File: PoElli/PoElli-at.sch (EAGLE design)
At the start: 119 parts, among them J1 DF12-60DP, Q1 FDV301N, Q2 SI1307DL, T1 POE-ISOLATION, U1 FST3257, U3 NCP1117, X1 RJ45MOLEX, Y1 25MHz

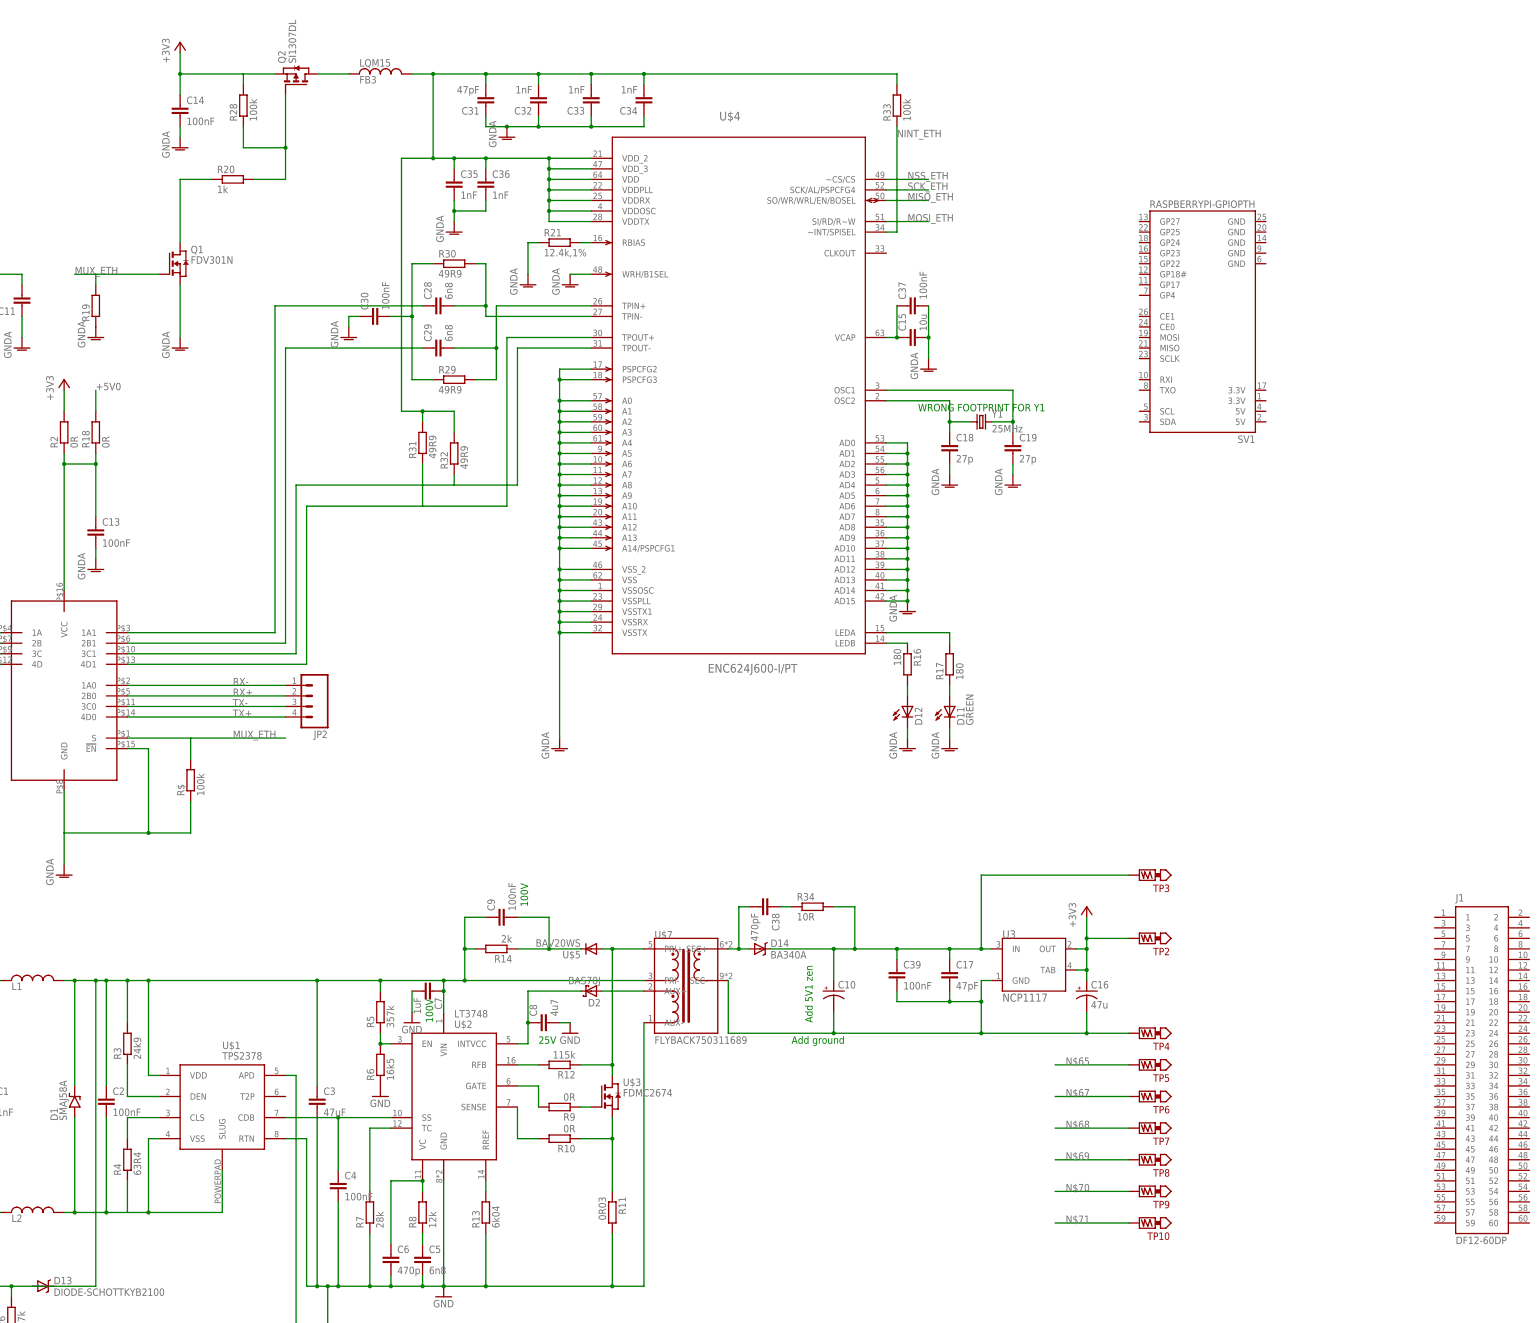
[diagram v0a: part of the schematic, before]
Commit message: Update and add wiring for ELL-i and RasPi connectors
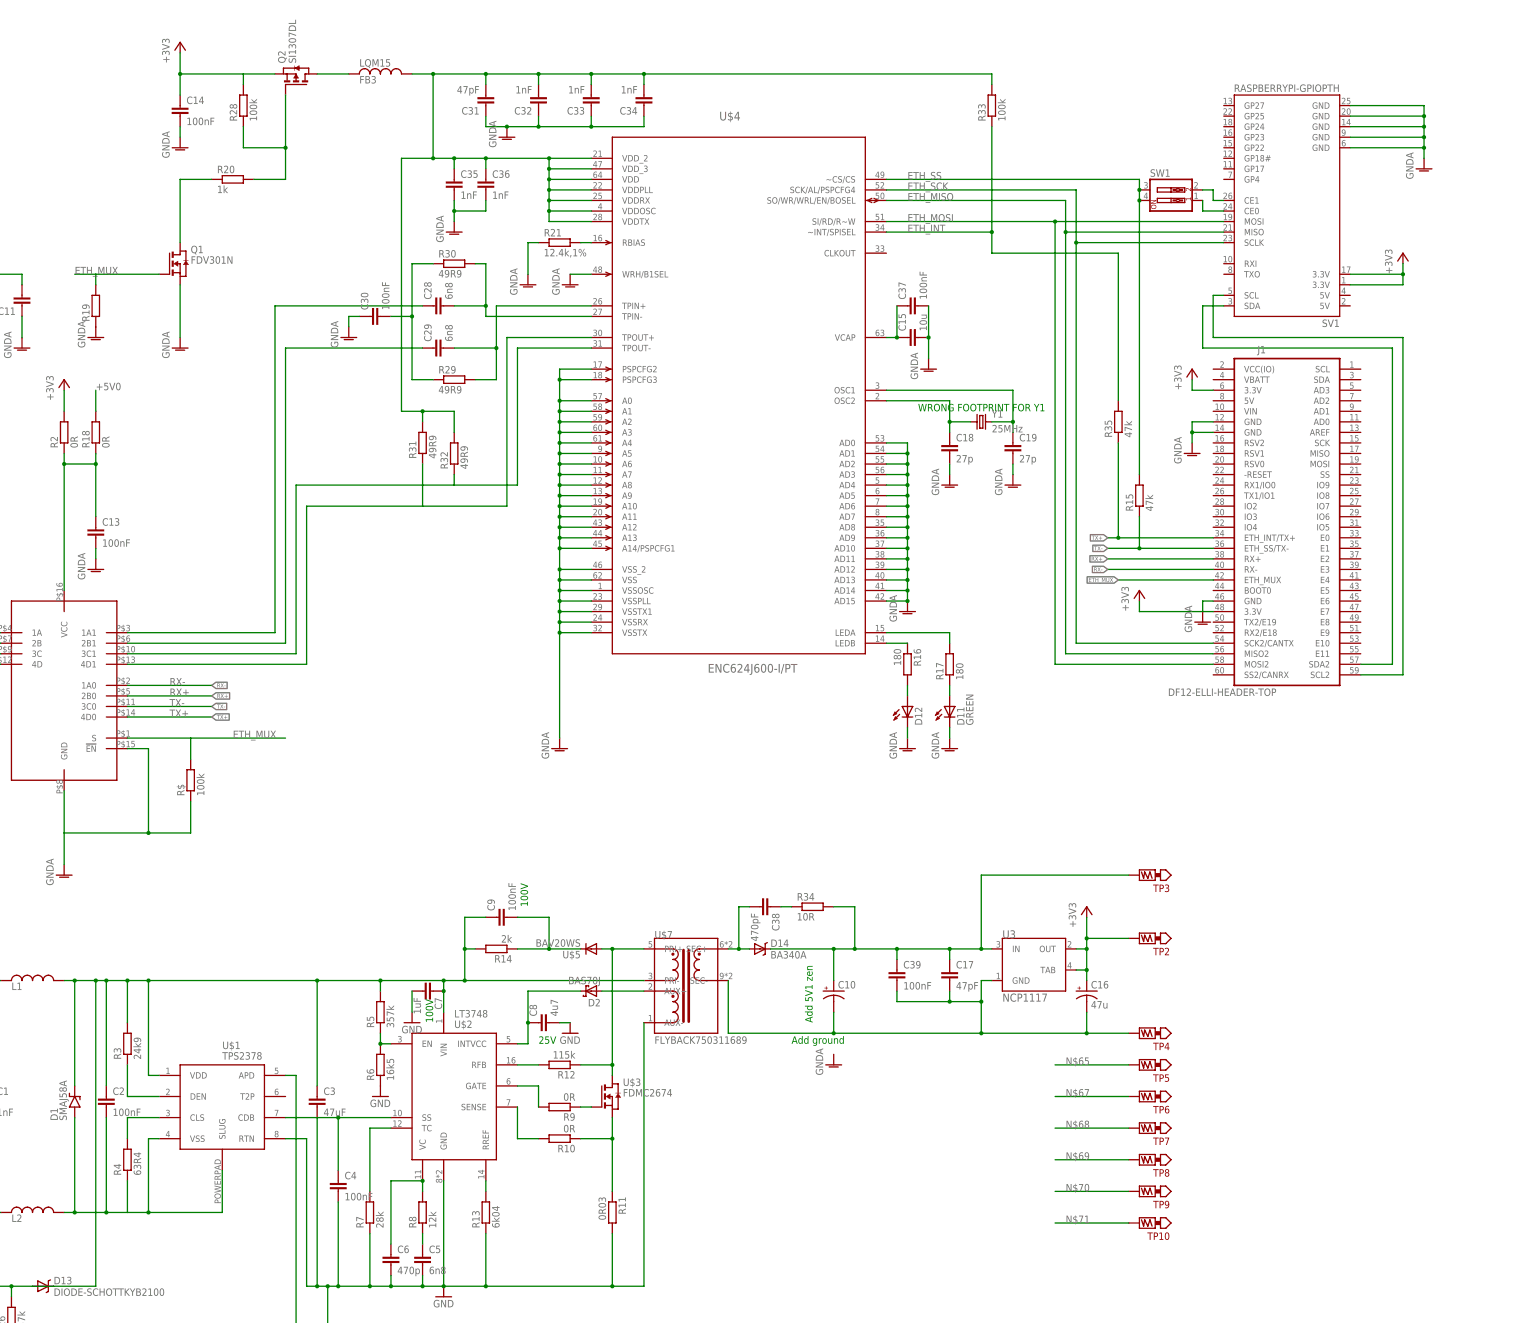
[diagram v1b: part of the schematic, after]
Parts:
- removed JP2: (no value), SparkFun-Connectors:M04LOCK
- added R15, R35: 47k, ELL-i-Passives:R0805
- added SW1: (no value), SparkFun-Electromechanical:SW_DIP-2-SMT-HALFSIZE
- J1: value DF12-60DP -> DF12-ELLI-HEADER-TOP; device ELL-i-Connectors:DF12-60DP -> ELL-i-Connectors:DF12-ELLI-HEADER-TOP
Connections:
- removed net MISO_ETH: U$4.SO/WR/WRL/EN/BOSEL
- removed net MOSI_ETH: U$4.SI/RD/R~W
- removed net MUX_ETH: Q1.G, R$.2, R19.2, U1.S
- removed net NINT_ETH: R33.1, U$4.~INT/SPISEL
- removed net NSS_ETH: U$4.~CS/CS
- removed net SCK_ETH: U$4.SCK/AL/PSPCFG4
- new net ETH_INT: R33.1, R35.2, U$4.~INT/SPISEL
- new net ETH_MISO: J1.MISO2, SV1.MISO, U$4.SO/WR/WRL/EN/BOSEL
- new net ETH_MOSI: J1.MOSI2, SV1.MOSI, U$4.SI/RD/R~W
- new net ETH_MUX: J1.ETH_MUX, Q1.G, R$.2, R19.2, U1.S
- new net ETH_SCK: J1.SCK2/CANTX, SV1.SCLK, U$4.SCK/AL/PSPCFG4
- new net ETH_SS: R15.2, SW1.3, SW1.4, U$4.~CS/CS
- new net N$72: J1.SDA2, SV1.SDA
- new net N$73: J1.SCL2, SV1.SCL
- new net N$74: SV1.CE1, SW1.2
- new net N$75: SV1.CE0, SW1.1
- net +3V3: now also J1.3.3V@48, J1.3.3V@6, SV1.3.3V@1, SV1.3.3V@17
- net GNDA: now also J1.GND@12, J1.GND@14, J1.GND@46, SV1.GND@14, SV1.GND@20, SV1.GND@25, SV1.GND@6, SV1.GND@9
- net RX+: now also J1.RX+; no longer JP2.2
- net RX-: now also J1.RX-; no longer JP2.1
- net TX+: now also J1.ETH_INT/TX+, R35.1; no longer JP2.4
- net TX-: now also J1.ETH_SS/TX-, R15.1; no longer JP2.3
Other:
- moved on the sheet: R33, SV1

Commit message: Cleanup PoElli-at aka Piwelli
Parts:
- D13: value DIODE-SCHOTTKYB2100 -> B2100
- T1: value POE-ISOLATION -> POE-ISOLATION-230NL; device ELL-i-Transformers:POE-ISOLATION -> ELL-i-Transformers:POE-ISOLATION-230NL
- X1: value RJ45MOLEX -> POE-TP-RJ45-MOLEX; device ELL-i-Connectors:RJ45MOLEX -> ELL-i-Connectors:POE-TP-RJ45-MOLEX
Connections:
- new net N$76: C26.1, D13.A, FB1.2, R26.2
- net N$1: now also T1.TX-, X1.TX-@2; no longer T1.TX1-, X1.2
- net N$16: no longer C26.1, D13.A, FB1.2, R26.2
- net N$2: now also T1.TX+, X1.TX+@1; no longer T1.TX1+, X1.1
- net N$3: now also T1.RX+, X1.RX+@3; no longer T1.RX1+, X1.3
- net N$4: now also X1.RX-@6; no longer X1.6
- net N$5: now also X1.POE-@7, X1.POE-@8; no longer X1.7, X1.8
- net N$7: now also X1.POE+@4, X1.POE+@5; no longer X1.4, X1.5
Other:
- moved on the sheet: C1, C10, C11, C12, C13, C14, C16, C17, C2, C20, C21, C22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

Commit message: Small fixes to PoElli
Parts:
- T1: value POE-ISOLATION-230NL -> Coilcraft 230NL
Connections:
- net +3V3: no longer SV1.3.3V@1, SV1.3.3V@17
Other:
- note added: "How about VCC(IO)? Set by MCU?"
- note added: "RasPi 3.3V must float"
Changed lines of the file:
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@@
 <part name="U$1" library="ELL-i-PowerIC" deviceset="TPS2378" device=""/>
 <part name="X1" library="ELL-i-Connectors" deviceset="POE-TP" device="-RJ45-MOLEX"/>
-<part name="T1" library="ELL-i-Transformers" deviceset="POE-ISOLATION" device="-230NL"/>
+<part name="T1" library="ELL-i-Transformers" deviceset="POE-ISOLATION" device="-230NL" value="Coilcraft 230NL"/>
 <part name="SV1" library="SparkFun-Boards" deviceset="RASPBERRYPI-GPIO" device="PTH"/>
 <part name="C1" library="ELL-i-Passives" deviceset="C" device="0805" value="1nF"/>
@@
 <part name="GND26" library="supply1" deviceset="GNDA" device=""/>
 <part name="GND27" library="supply1" deviceset="GNDA" device=""/>
-<part name="+3V5" library="supply1" deviceset="+3V3" device=""/>
 <part name="+3V6" library="supply1" deviceset="+3V3" device=""/>
 <part name="+3V7" library="supply1" deviceset="+3V3" device=""/>
@@
 <text x="322.58" y="73.66" size="1.778" layer="91">Add ground</text>
 <text x="327.66" y="78.74" size="1.778" layer="91" rot="R90">Add 5V1 zen</text>
+<text x="347.98" y="261.62" size="1.778" layer="97" align="center">RasPi 3.3V
+must float </text>
+<text x="294.64" y="243.84" size="1.778" layer="97" align="center">How about
+VCC(IO)?
+Set by MCU?</text>
 </plain>
 <instances>
@@
 <instance part="GND26" gate="1" x="302.26" y="177.8"/>
 <instance part="GND27" gate="1" x="299.72" y="218.44"/>
-<instance part="+3V5" gate="G$1" x="350.52" y="266.7"/>
 <instance part="+3V6" gate="G$1" x="299.72" y="238.76"/>
 <instance part="+3V7" gate="G$1" x="287.02" y="185.42"/>
@@
 </segment>
 <segment>
-<pinref part="SV1" gate="JP1" pin="3.3V@17"/>
-<wire x1="337.82" y1="261.62" x2="350.52" y2="261.62" width="0.1524" layer="91"/>
-<pinref part="+3V5" gate="G$1" pin="+3V3"/>
-<wire x1="350.52" y1="261.62" x2="350.52" y2="264.16" width="0.1524" layer="91"/>
-<pinref part="SV1" gate="JP1" pin="3.3V@1"/>
-<wire x1="337.82" y1="259.08" x2="350.52" y2="259.08" width="0.1524" layer="91"/>
-<wire x1="350.52" y1="259.08" x2="350.52" y2="261.62" width="0.1524" layer="91"/>
-<junction x="350.52" y="261.62"/>
-</segment>
-<segment>
 <pinref part="J1" gate="E" pin="3.3V@6"/>
 <wire x1="304.8" y1="233.68" x2="299.72" y2="233.68" width="0.1524" layer="91"/>
@@
 </schematic>
 </drawing>
+<compatibility>
+<note version="6.3" minversion="6.2.2" severity="warning">
+Since Version 6.2.2 text objects can contain more than one line,
+which will not be processed correctly with this version.
+</note>
+</compatibility>
 </eagle>

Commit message: Update connector connections
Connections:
- net ETH_SS renamed N$35
- removed net N$35 (its old number): C10.+, C17.1, C39.1, D14.C, R34.2, TP3.P$1, U3.IN
- removed net N$75: SV1.CE0, SW1.1
- new net 5V: C10.+, C17.1, C39.1, D14.C, J1.5V, R34.2, SV1.5V@2, SV1.5V@4, TP3.P$1, U3.IN
- new net ENC-3V3: C31.2, C32.2, C33.2, C34.2, C35.1, C36.1, FB3.2, R31.2, R32.2, R33.2, U$4.VDD, U$4.VDDOSC, U$4.VDDPLL, U$4.VDDRX, U$4.VDDTX, U$4.VDD_2, U$4.VDD_3
- new net SS2: J1.SS2/CANRX, SV1.CE0, SW1.1
- net +3V3: now also C16.+, TP2.P$1, U3.OUT, U3.TAB
- net +5V0: no longer C16.+, C31.2, C32.2, C33.2, C34.2, C35.1, C36.1, FB3.2, R31.2, R32.2, R33.2, TP2.P$1, U$4.VDD, U$4.VDDOSC, U$4.VDDPLL, U$4.VDDRX, U$4.VDDTX, U$4.VDD_2, U$4.VDD_3, U3.OUT, U3.TAB
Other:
- note added: "VCC(IO) left open"
- note removed: "How about VCC(IO)? Set by MCU?"
- moved on the sheet: C14, FB3, Q1, Q2, R15, R19, R20, R28, R35, SW1

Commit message: Move BAV20WS to Ell-i-DiscreteSemi.lbr
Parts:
- removed U$5: BAV20WS, TPS2378:BAV20WS
- added D15: BAV20WS, ELL-i-DIscreteSemi:BAV20WS
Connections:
- net N$28: now also D15.A; no longer U$5.A
- net N$33: now also D15.C; no longer U$5.C
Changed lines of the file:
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@@
 <part name="GND5" library="ell-i" deviceset="GND" device=""/>
 <part name="R13" library="ELL-i-Passives" deviceset="R" device="0402" value="6k04"/>
-<part name="U$5" library="TPS2378" deviceset="BAV20WS" device=""/>
+<part name="D15" library="ELL-i-DIscreteSemi" deviceset="BAV20WS" device=""/>
 <part name="R14" library="ELL-i-Passives" deviceset="R" device="0805" value="2k"/>
 <part name="C9" library="ELL-i-Passives" deviceset="C" device="0805" value="100nF"/>
@@
 <instance part="GND5" gate="1" x="269.24" y="76.2"/>
 <instance part="R13" gate="G$1" x="248.92" y="33.02" rot="R90"/>
-<instance part="U$5" gate="G$1" x="274.32" y="96.52" rot="R180"/>
+<instance part="D15" gate="G$1" x="274.32" y="96.52" rot="R180"/>
 <instance part="R14" gate="G$1" x="251.46" y="96.52" rot="R180"/>
 <instance part="C9" gate="G$1" x="251.46" y="104.14" rot="R90"/>
@@
 <wire x1="271.78" y1="68.58" x2="279.4" y2="68.58" width="0.1524" layer="91"/>
 <junction x="279.4" y="68.58"/>
-<pinref part="U$5" gate="G$1" pin="A"/>
+<pinref part="D15" gate="G$1" pin="A"/>
 <wire x1="276.86" y1="96.52" x2="279.4" y2="96.52" width="0.1524" layer="91"/>
 <junction x="279.4" y="96.52"/>
@@
 <pinref part="C9" gate="G$1" pin="2"/>
 <wire x1="264.16" y1="104.14" x2="256.54" y2="104.14" width="0.1524" layer="91"/>
-<pinref part="U$5" gate="G$1" pin="C"/>
+<pinref part="D15" gate="G$1" pin="C"/>
 <wire x1="271.78" y1="96.52" x2="264.16" y2="96.52" width="0.1524" layer="91"/>
 <wire x1="264.16" y1="104.14" x2="264.16" y2="96.52" width="0.1524" layer="91"/>

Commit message: Manually renamed PoElli components other than R,C,D
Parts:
- removed L1, L2: (no value), ELL-i-Passives:FB
- removed U$4: ENC624J600-I/PT, ELL-i-DigitalIC:ENC624J600-I/PT
- added FB4, FB5: 2A, ELL-i-Passives:FB
- added U2: NCP1117, ell-i:NCP1117
- FB1: value 2A -> LQM15
- FB2: value 2A -> (none)
- FB3: value LQM15 -> (none)
- Q1: value FDV301N -> SI1307DL; device ELL-i-DIscreteSemi:FDV301N -> ELL-i-DIscreteSemi:SI1307DL
- Q2: value SI1307DL -> FDV301N; device ELL-i-DIscreteSemi:SI1307DL -> ELL-i-DIscreteSemi:FDV301N
- U1: value FST3257 -> ENC624J600-I/PT; device ELL-i-DigitalIC:FST3257 -> ELL-i-DigitalIC:ENC624J600-I/PT
- U3: value NCP1117 -> FST3257; device ell-i:NCP1117 -> ELL-i-DigitalIC:FST3257
- renumbered U$1 to U5, U$2 to U4, U$3 to Q3, U$7 to T2
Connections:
- net +3V3: now also Q1.S, U2.OUT, U2.TAB; no longer Q2.S, U3.OUT, U3.TAB
- net 5V: now also U2.IN; no longer U3.IN
- net ENC-3V3: now also FB1.2, U1.VDD, U1.VDDOSC, U1.VDDPLL, U1.VDDRX, U1.VDDTX, U1.VDD_2, U1.VDD_3; no longer FB3.2, U$4.VDD, U$4.VDDOSC, U$4.VDDPLL, U$4.VDDRX, U$4.VDDTX, U$4.VDD_2, U$4.VDD_3
- net ETH_INT: now also U1.~INT/SPISEL; no longer U$4.~INT/SPISEL
- net ETH_MISO: now also U1.SO/WR/WRL/EN/BOSEL; no longer U$4.SO/WR/WRL/EN/BOSEL
- net ETH_MOSI: now also U1.SI/RD/R~W; no longer U$4.SI/RD/R~W
- net ETH_MUX: now also Q2.G, U3.S; no longer Q1.G, U1.S
- net ETH_SCK: now also U1.SCK/AL/PSPCFG4; no longer U$4.SCK/AL/PSPCFG4
- net GND: now also FB5.2; no longer FB2.2
- net GNDA: now also Q2.S, U1.A0, U1.A1, U1.A10, U1.A11, U1.A12, U1.A13, U1.A14/PSPCFG1, U1.A2, U1.A3, U1.A4, U1.A5, U1.A6, U1.A7, U1.A8, U1.A9, U1.AD0, U1.AD1, U1.AD10, U1.AD11, U1.AD12, U1.AD13, U1.AD14, U1.AD15, U1.AD2, U1.AD3, U1.AD4, U1.AD5, U1.AD6, U1.AD7, U1.AD8, U1.AD9, U1.PSPCFG2, U1.PSPCFG3, U1.VSS, U1.VSSOSC, U1.VSSPLL, U1.VSSRX, U1.VSSTX, U1.VSSTX1, U1.VSS_2, U1.WRH/B1SEL, U3.!EN, U3.GND; no longer Q1.S, U$4.A0, U$4.A1, U$4.A10, U$4.A11, U$4.A12, U$4.A13, U$4.A14/PSPCFG1, U$4.A2, U$4.A3, U$4.A4, U$4.A5, U$4.A6, U$4.A7, U$4.A8, U$4.A9, U$4.AD0, U$4.AD1, U$4.AD10, U$4.AD11, U$4.AD12, U$4.AD13, U$4.AD14, U$4.AD15, U$4.AD2, U$4.AD3, U$4.AD4, U$4.AD5, U$4.AD6, U$4.AD7, U$4.AD8, U$4.AD9, U$4.PSPCFG2, U$4.PSPCFG3, U$4.VSS, U$4.VSSOSC, U$4.VSSPLL, U$4.VSSRX, U$4.VSSTX, U$4.VSSTX1, U$4.VSS_2, U$4.WRH/B1SEL, U1.!EN, U1.GND
- net N$11: now also U3.4D; no longer U1.4D
- net N$12: now also U3.3C; no longer U1.3C
- net N$13: now also U3.2B; no longer U1.2B
- net N$14: now also U3.1A; no longer U1.1A
- net N$15: now also FB3.2; no longer L2.2
- net N$16: now also FB2.2; no longer L1.2
- net N$35: now also U1.~CS/CS; no longer U$4.~CS/CS
- net N$37: now also U1.OSC2; no longer U$4.OSC2
- net N$39: now also U1.TPIN-; no longer U$4.TPIN-
- net N$41: now also U1.LEDB; no longer U$4.LEDB
- net N$42: now also U1.LEDA; no longer U$4.LEDA
- net N$43: now also U3.VCC; no longer U1.VCC
- net N$45: now also U1.RBIAS; no longer U$4.RBIAS
- net N$46: now also U1.VCAP; no longer U$4.VCAP
- net N$47: now also U1.OSC1; no longer U$4.OSC1
- net N$53: now also FB4.1; no longer FB1.1
- net N$55: now also FB5.1; no longer FB2.1
- net N$56: now also Q2.D; no longer Q1.D
- net N$57: now also Q1.G; no longer Q2.G
- net N$58: now also U2.GND; no longer U3.GND
- net N$59: now also U1.TPIN+; no longer U$4.TPIN+
- net N$6: now also FB2.1; no longer L1.1
- net N$60: now also FB1.1, Q1.D; no longer FB3.1, Q2.D
- net N$61: now also U3.1A1; no longer U1.1A1
- net N$62: now also U1.TPOUT+, U3.4D1; no longer U$4.TPOUT+, U1.4D1
- net N$63: now also U1.TPOUT-, U3.3C1; no longer U$4.TPOUT-, U1.3C1
- net N$64: now also U3.2B1; no longer U1.2B1
- net N$76: now also FB4.2; no longer FB1.2
- net N$8: now also FB3.1; no longer L2.1
- net RX+: now also U3.2B0; no longer U1.2B0
- net RX-: now also U3.1A0; no longer U1.1A0
- net TX+: now also U3.4D0; no longer U1.4D0
- net TX-: now also U3.3C0; no longer U1.3C0
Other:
- moved on the sheet: FB1, FB2, FB3, Q1, Q2

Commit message: Renamed R,C,D in PoElli
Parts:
- renumbered C1 to XXC1XX, C10 to XXC10XX, C11 to XXC11XX, C12 to XXC12XX, C13 to XXC13XX, C14 to XXC14XX, C15 to XXC15XX, C16 to XXC16XX, C17 to XXC17XX, C18 to XXC18XX, C19 to XXC19XX, C2 to XXC2XX, C20 to XXC20XX, C21 to XXC21XX, C22 to XXC22XX, C23 to XXC23XX, C24 to XXC24XX, C25 to XXC25XX, C26 to XXC26XX, C27 to XXC27XX, C28 to XXC28XX, C29 to XXC29XX, C3 to XXC3XX, C30 to XXC30XX, C31 to XXC31XX, C32 to XXC32XX, C33 to XXC33XX, C34 to XXC34XX, C35 to XXC35XX, C36 to XXC36XX, C37 to XXC37XX, C38 to XXC38XX, C39 to XXC39XX, C4 to XXC4XX, C5 to XXC5XX, C6 to XXC6XX, C7 to XXC7XX, C8 to XXC8XX, C9 to XXC9XX, D1 to XXD1XX, D10 to XXD10XX, D11 to XXD11XX, D12 to XXD12XX, D13 to XXD13XX, D14 to XXD14XX, D15 to XXD15XX, D2 to XXD2XX, D3 to XXD3XX, D4 to XXD4XX, D5 to XXD5XX, D6 to XXD6XX, D7 to XXD7XX, D8 to XXD8XX, D9 to XXD9XX, R1 to XXR1XX, R10 to XXR10XX, R11 to XXR11XX, R12 to XXR12XX, R13 to XXR13XX, R14 to XXR14XX, R15 to XXR15XX, R16 to XXR16XX, R17 to XXR17XX, R18 to XXR18XX, R19 to XXR19XX, R2 to XXR2XX, R20 to XXR20XX, R21 to XXR21XX, R22 to XXR22XX, R23 to XXR23XX, R24 to XXR24XX, R25 to XXR25XX, R26 to XXR26XX, R27 to XXR27XX, R28 to XXR28XX, R29 to XXR29XX, R3 to XXR3XX, R30 to XXR30XX, R31 to XXR31XX, R32 to XXR32XX, R33 to XXR33XX, R34 to XXR34XX, R35 to XXR35XX, R4 to XXR4XX, R5 to XXR5XX, R6 to XXR6XX, R7 to XXR7XX, R8 to XXR8XX, R9 to XXR9XX

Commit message: Fix previous commit screwups + cleanups to PoElli
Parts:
- removed XXC11XX: (no value), ELL-i-Passives:C0805
- removed XXC1XX, XXC24XX: 1nF, ELL-i-Passives:C0805
- removed XXC20XX, XXC21XX, XXC22XX, XXC23XX: 10nF, ELL-i-Passives:C0805
- removed XXC28XX, XXC29XX: 6n8, ELL-i-Passives:C0805
- removed XXD10XX, XXD13XX, XXD3XX, XXD4XX, XXD5XX, XXD6XX, XXD7XX, XXD8XX, XXD9XX: B2100, ELL-i-DIscreteSemi:DIODE-SCHOTTKYB2100
- removed XXD1XX: SMAJ58A, ell-i:SMAJ58A
- removed XXR1XX: (no value), ELL-i-Passives:R0805
- removed XXR22XX, XXR23XX, XXR24XX, XXR25XX: 75R, ELL-i-Passives:R0805
- removed XXR29XX: 49R9, ELL-i-Passives:R0805
- added C10, C24, C25, C26, C27: 10nF, ELL-i-Passives:C0805
- added C11, C15: 6n8, ELL-i-Passives:C0805
- added C31, C34: 1nF, ELL-i-Passives:C0805
- added D10, D14, D15, D16, D17, D18, D7, D8, D9: B2100, ELL-i-DIscreteSemi:DIODE-SCHOTTKYB2100
- added D12: SMAJ58A, ell-i:SMAJ58A
- added R18, R19, R20, R21: 75R, ELL-i-Passives:R0805
- added R5: 10R, ELL-i-Passives:R0805
- added R9: 49R9, ELL-i-Passives:R0805
- C19: value (none) -> 10nF
- R7: value (none) -> 10K
- renumbered R$ to R17, XXC10XX to C23, XXC12XX to C19, XXC13XX to C20, XXC14XX to C3, XXC15XX to C13, XXC16XX to C16, XXC17XX to C18, XXC18XX to C1, XXC19XX to C2, XXC25XX to C40, XXC26XX to C41, XXC27XX to C42, XXC2XX to C35, XXC30XX to C12, XXC31XX to C4, XXC32XX to C5, XXC33XX to C6, XXC34XX to C7, XXC35XX to C8, XXC36XX to C9, XXC37XX to C14, XXC38XX to C22, XXC39XX to C17, XXC3XX to C32, XXC4XX to C37, XXC5XX to C39, XXC6XX to C38, XXC7XX to C29, XXC8XX to C30, XXC9XX to C21, XXD11XX to D2, XXD12XX to D1, XXD14XX to D4, XXD15XX to D3, XXD2XX to D6, XXR10XX to R30, XXR11XX to R32, XXR12XX to R24, XXR13XX to R34, XXR14XX to R16, XXR15XX to R37, XXR16XX to R4, XXR17XX to R3, XXR18XX to R11, XXR19XX to R7, XXR20XX to R2, XXR21XX to R6, XXR26XX to R35, XXR27XX to R36, XXR28XX to R1, XXR2XX to R10, XXR30XX to R8, XXR31XX to R13, XXR32XX to R12, XXR33XX to R14, XXR34XX to R15, XXR3XX to R23, XXR4XX to R29, XXR5XX to R22, XXR6XX to R26, XXR7XX to R31, XXR8XX to R33, XXR9XX to R28
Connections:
- removed net N$10: T1.TXCT, XXC23XX.1, XXD10XX.A, XXD6XX.C
- removed net N$49: XXC24XX.1, XXR22XX.1, XXR23XX.1, XXR24XX.1, XXR25XX.1
- removed net N$61: U3.1A1, XXC28XX.1
- removed net N$62: R13.1, U1.TPOUT+, U3.4D1
- removed net N$63: R12.1, U1.TPOUT-, U3.3C1
- removed net N$64: U3.2B1, XXC29XX.1
- removed net N$7: X1.POE+@4, X1.POE+@5, XXC20XX.1, XXD3XX.C, XXD7XX.A
- removed net N$9: T1.RXCT, XXC22XX.1, XXD5XX.C, XXD9XX.A
- new net POE_A+: C24.1, D14.C, D7.A, T1.TXCT
- new net POE_A-: C25.1, D15.C, D8.A, T1.RXCT
- new net POE_B+: C27.1, D10.A, D17.C, X1.POE+@4, X1.POE+@5
- new net POE_B-: C26.1, D16.C, D9.A, X1.POE-@7, X1.POE-@8
- new net TPIN+: C15.1, U3.2B1
- new net TPIN-: C11.1, U3.1A1
- new net TPOUT+: R12.1, U1.TPOUT-, U3.4D1
- new net TPOUT-: R13.1, U1.TPOUT+, U3.3C1
- net +3V3: now also R5.2; no longer XXR1XX.2
- net GNDA: now also C10.1; no longer XXC11XX.1
- net N$15: now also D12.A; no longer XXD1XX.A
- net N$16: now also D12.C, D18.C; no longer XXD13XX.C, XXD1XX.C
- net N$39: now also C11.2; no longer XXC28XX.2
- net N$40: now also C10.2, R5.1, T1.RCT; no longer XXC11XX.2, XXR1XX.1
- net N$44: now also R9.1; no longer XXR29XX.1
- net N$48: now also C27.2, R21.2; no longer XXC20XX.2, XXR22XX.2
- net N$5: now also C31.1, R18.1, R19.1, R20.1, R21.1; no longer X1.POE-@7, X1.POE-@8, XXC21XX.1, XXD4XX.C, XXD8XX.A
- net N$50: now also C24.2, R18.2; no longer XXC23XX.2, XXR25XX.2
- net N$51: now also C25.2, R19.2; no longer XXC22XX.2, XXR24XX.2
- net N$52: now also C26.2, R20.2; no longer XXC21XX.2, XXR23XX.2
- net N$59: now also C15.2, R9.2; no longer XXC29XX.2, XXR29XX.2
- net N$6: now also C34.1, D10.C, D7.C, D8.C, D9.C; no longer XXC1XX.1, XXD10XX.C, XXD7XX.C, XXD8XX.C, XXD9XX.C
- net N$76: now also D18.A; no longer XXD13XX.A
- net N$8: now also C34.2, D14.A, D15.A, D16.A, D17.A; no longer XXC1XX.2, XXD3XX.A, XXD4XX.A, XXD5XX.A, XXD6XX.A
- net SGND: now also C31.2; no longer XXC24XX.2
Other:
- moved on the sheet: FB2, FB3, TP1
